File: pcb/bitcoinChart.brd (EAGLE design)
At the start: 59.7 x 53.3 mm, 35 parts, among them SW5 KMR2, SW6 KMR2, U2 MPU-6050, U7 SPX3819

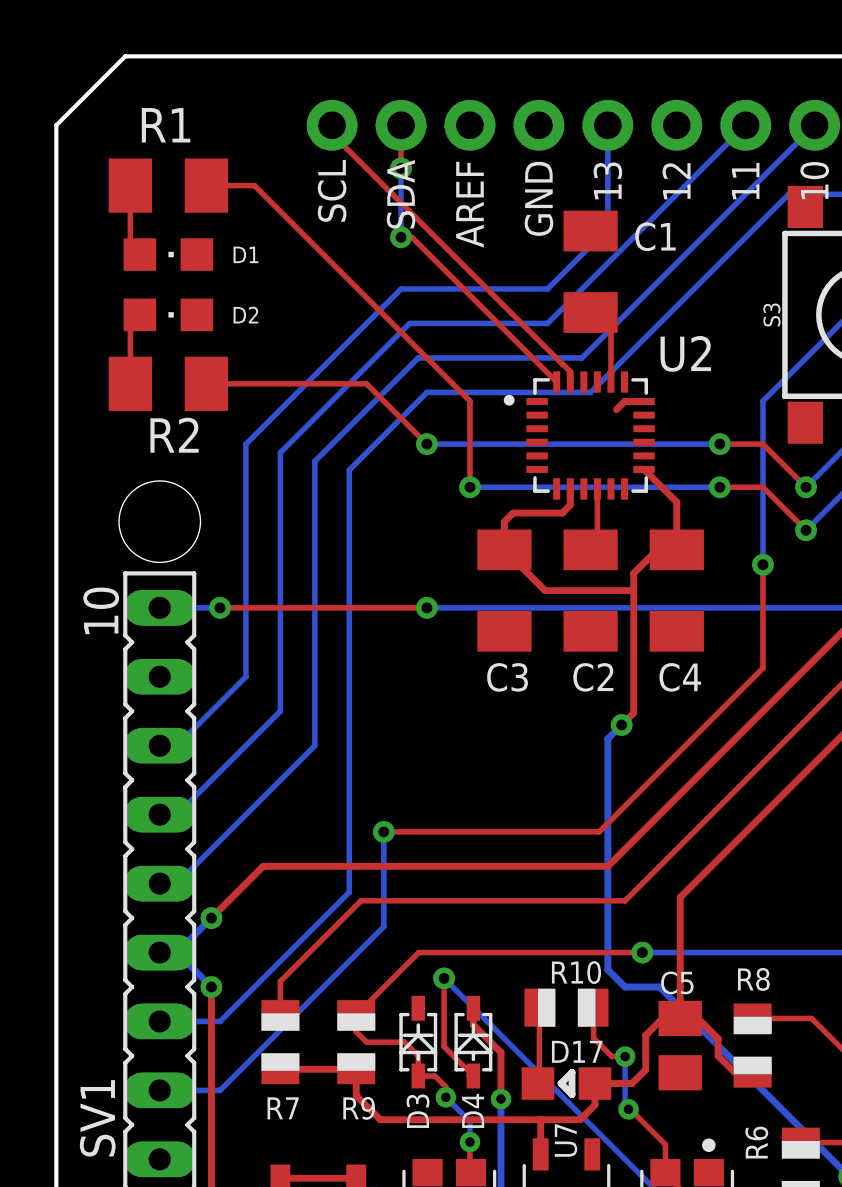
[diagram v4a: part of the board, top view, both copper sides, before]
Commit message: Added MISO
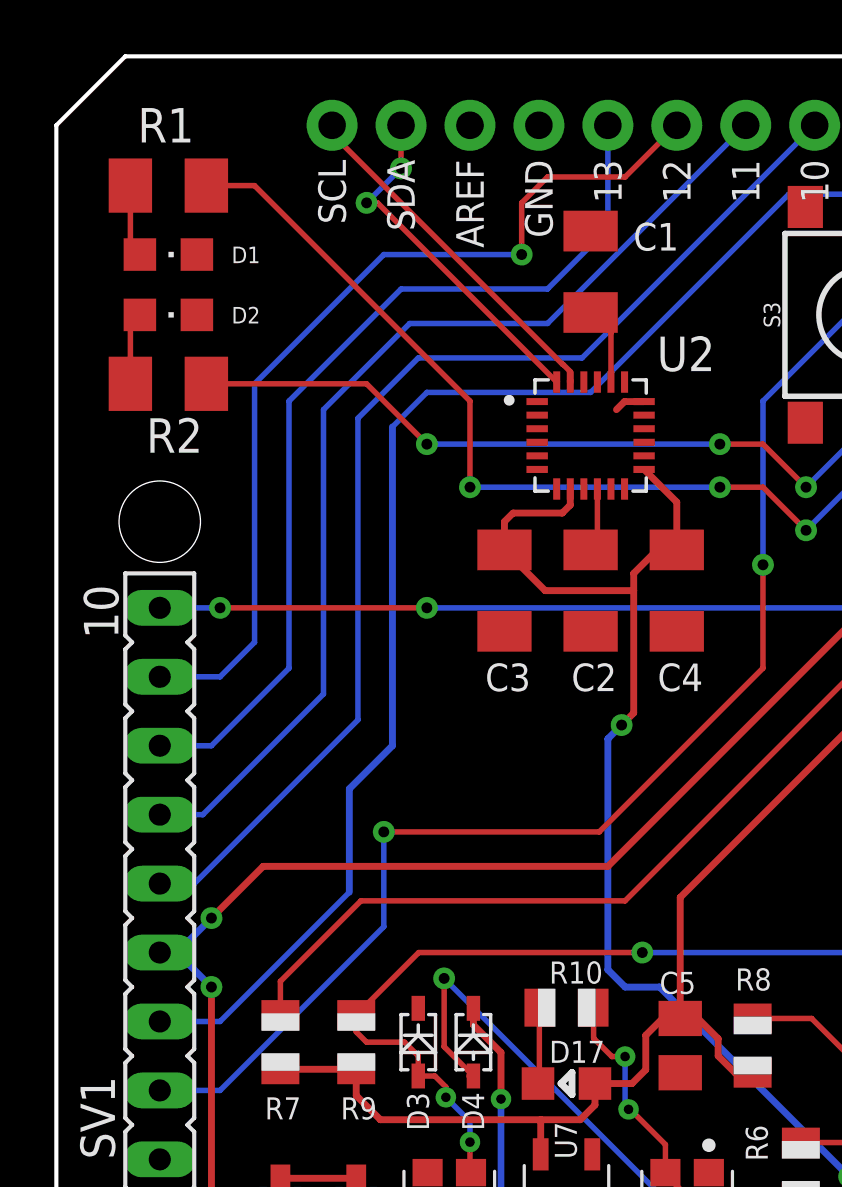
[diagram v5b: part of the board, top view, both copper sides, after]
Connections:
- new net N$12: B1.D12, SV1.9
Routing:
- net N$12: track 0.00 -> 34.2 mm, vias 0 -> 1
- net N$3: track 12.1 -> 13.2 mm
- net N$6: track 33.2 -> 34.0 mm
- net N$7: track 38.3 -> 38.9 mm
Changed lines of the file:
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@@
 <contactref element="B1" pad="D13"/>
 <contactref element="SV1" pad="8"/>
-<wire x1="102.87" y1="39.37" x2="103.505" y2="39.37" width="0.2032" layer="16"/>
-<wire x1="106.045" y1="41.91" x2="103.505" y2="39.37" width="0.2032" layer="16"/>
+<wire x1="102.87" y1="39.37" x2="104.775" y2="39.37" width="0.2032" layer="16"/>
+<wire x1="107.6325" y1="42.2275" x2="104.775" y2="39.37" width="0.2032" layer="16"/>
 <wire x1="119.38" y1="62.23" x2="119.38" y2="58.42" width="0.2032" layer="16"/>
 <wire x1="119.38" y1="58.42" x2="117.1575" y2="56.1975" width="0.2032" layer="16"/>
-<wire x1="111.76" y1="56.1975" x2="106.045" y2="50.4825" width="0.2032" layer="16"/>
+<wire x1="111.76" y1="56.1975" x2="107.6325" y2="52.07" width="0.2032" layer="16"/>
 <wire x1="117.1575" y1="56.1975" x2="111.76" y2="56.1975" width="0.2032" layer="16"/>
-<wire x1="106.045" y1="50.4825" x2="106.045" y2="41.91" width="0.2032" layer="16"/>
+<wire x1="107.6325" y1="52.07" x2="107.6325" y2="42.2275" width="0.2032" layer="16"/>
 </signal>
 <signal name="N$7">
@@
 <contactref element="SV1" pad="7"/>
 <via x="102.87" y="36.83" extent="1-16" drill="0.4"/>
-<wire x1="102.87" y1="36.83" x2="103.505" y2="36.83" width="0.2032" layer="16"/>
-<wire x1="107.315" y1="40.64" x2="103.505" y2="36.83" width="0.2032" layer="16"/>
+<wire x1="102.87" y1="36.83" x2="104.4575" y2="36.83" width="0.2032" layer="16"/>
+<wire x1="108.9025" y1="41.275" x2="104.4575" y2="36.83" width="0.2032" layer="16"/>
 <wire x1="124.46" y1="61.595" x2="124.46" y2="62.23" width="0.2032" layer="16"/>
 <wire x1="124.46" y1="62.23" x2="117.1575" y2="54.9275" width="0.2032" layer="16"/>
 <wire x1="117.1575" y1="54.9275" x2="112.0775" y2="54.9275" width="0.2032" layer="16"/>
-<wire x1="112.0775" y1="54.9275" x2="107.315" y2="50.165" width="0.2032" layer="16"/>
-<wire x1="107.315" y1="50.165" x2="107.315" y2="40.64" width="0.2032" layer="16"/>
+<wire x1="112.0775" y1="54.9275" x2="108.9025" y2="51.7525" width="0.2032" layer="16"/>
+<wire x1="108.9025" y1="51.7525" x2="108.9025" y2="41.275" width="0.2032" layer="16"/>
 </signal>
 <signal name="N$8">
 <contactref element="B1" pad="D10"/>
 <contactref element="SV1" pad="6"/>
-<wire x1="102.87" y1="34.29" x2="103.505" y2="34.29" width="0.2032" layer="16"/>
-<wire x1="108.585" y1="39.37" x2="103.505" y2="34.29" width="0.2032" layer="16"/>
+<wire x1="102.87" y1="34.29" x2="104.14" y2="34.29" width="0.2032" layer="16"/>
+<wire x1="110.1725" y1="40.3225" x2="104.14" y2="34.29" width="0.2032" layer="16"/>
 <wire x1="127" y1="62.23" x2="118.4275" y2="53.6575" width="0.2032" layer="16"/>
 <wire x1="118.4275" y1="53.6575" x2="112.395" y2="53.6575" width="0.2032" layer="16"/>
-<wire x1="112.395" y1="53.6575" x2="108.585" y2="49.8475" width="0.2032" layer="16"/>
-<wire x1="108.585" y1="49.8475" x2="108.585" y2="39.37" width="0.2032" layer="16"/>
+<wire x1="112.395" y1="53.6575" x2="110.1725" y2="51.435" width="0.2032" layer="16"/>
+<wire x1="110.1725" y1="51.435" x2="110.1725" y2="40.3225" width="0.2032" layer="16"/>
 </signal>
 <signal name="N$9">
@@
 <contactref element="SV1" pad="4"/>
 <wire x1="102.87" y1="29.21" x2="105.0925" y2="29.21" width="0.2032" layer="16"/>
-<wire x1="109.855" y1="33.9725" x2="105.0925" y2="29.21" width="0.2032" layer="16"/>
+<wire x1="105.0925" y1="29.21" x2="109.855" y2="33.9725" width="0.2032" layer="16"/>
 <wire x1="128.27" y1="59.69" x2="126.0475" y2="59.69" width="0.2032" layer="16"/>
 <wire x1="128.27" y1="59.69" x2="129.54" y2="60.96" width="0.2032" layer="16"/>
@@
 <wire x1="126.0475" y1="59.69" x2="118.745" y2="52.3875" width="0.2032" layer="16"/>
 <wire x1="118.745" y1="52.3875" x2="112.7125" y2="52.3875" width="0.2032" layer="16"/>
-<wire x1="112.7125" y1="52.3875" x2="109.855" y2="49.53" width="0.2032" layer="16"/>
-<wire x1="109.855" y1="49.53" x2="109.855" y2="33.9725" width="0.2032" layer="16"/>
+<wire x1="112.7125" y1="52.3875" x2="111.4425" y2="51.1175" width="0.2032" layer="16"/>
+<wire x1="109.855" y1="33.9725" x2="109.855" y2="37.7825" width="0.254" layer="16"/>
+<wire x1="109.855" y1="37.7825" x2="111.4425" y2="39.37" width="0.254" layer="16"/>
+<wire x1="111.4425" y1="39.37" x2="111.4425" y2="51.1175" width="0.254" layer="16"/>
 </signal>
 <signal name="N$4">
@@
 <contactref element="B1" pad="SDA"/>
 <wire x1="117.495" y1="52.812" x2="117.495" y2="52.77" width="0.254" layer="1"/>
-<wire x1="117.495" y1="52.77" x2="112.1625" y2="58.1025" width="0.2032" layer="1"/>
-<wire x1="112.1625" y1="58.1025" x2="111.76" y2="58.1025" width="0.2032" layer="1"/>
-<via x="111.76" y="58.1025" extent="1-16" drill="0.4"/>
-<wire x1="111.76" y1="58.1025" x2="111.76" y2="60.6425" width="0.2032" layer="16"/>
+<wire x1="117.495" y1="52.77" x2="110.8925" y2="59.3725" width="0.2032" layer="1"/>
+<wire x1="110.8925" y1="59.3725" x2="110.49" y2="59.3725" width="0.2032" layer="1"/>
+<via x="110.49" y="59.3725" extent="1-16" drill="0.4"/>
+<wire x1="110.49" y1="59.3725" x2="111.76" y2="60.6425" width="0.2032" layer="16"/>
 <via x="111.76" y="60.6425" extent="1-16" drill="0.4"/>
 <wire x1="111.76" y1="60.6425" x2="111.76" y2="62.23" width="0.2032" layer="1"/>
@@
 </polygon>
 </signal>
+<signal name="N$12">
+<contactref element="B1" pad="D12"/>
+<contactref element="SV1" pad="9"/>
+<wire x1="102.87" y1="41.91" x2="105.0925" y2="41.91" width="0.2032" layer="16"/>
+<wire x1="105.0925" y1="41.91" x2="106.3625" y2="43.18" width="0.2032" layer="16"/>
+<wire x1="106.3625" y1="43.18" x2="106.3625" y2="52.705" width="0.2032" layer="16"/>
+<wire x1="111.125" y1="57.4675" x2="116.205" y2="57.4675" width="0.2032" layer="16"/>
+<via x="116.205" y="57.4675" extent="1-16" drill="0.4"/>
+<wire x1="116.205" y1="57.4675" x2="116.205" y2="59.3725" width="0.2032" layer="1"/>
+<wire x1="116.205" y1="59.3725" x2="117.1575" y2="60.325" width="0.2032" layer="1"/>
+<wire x1="117.1575" y1="60.325" x2="120.015" y2="60.325" width="0.2032" layer="1"/>
+<wire x1="120.015" y1="60.325" x2="121.92" y2="62.23" width="0.2032" layer="1"/>
+<wire x1="106.3625" y1="52.705" x2="111.125" y2="57.4675" width="0.2032" layer="16"/>
+</signal>
 </signals>
